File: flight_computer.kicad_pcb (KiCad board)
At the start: 4 copper layers, 95.9 x 90.2 mm, 163 parts, among them J1 436500204, J10 TSW-102-07-F-S, J11 TSW-103-07-F-S, J12 SMA-J-P-H-ST-EM1, J2 0530480210, J3 0530480210, J4 398800302, J5 398800302, J6 398800302, J7 398800302, J8 0530480810, J9 USB4105-GF-A-120, Q6 SI1016CX-T1-GE3, Q7 DMT6007LFGQ-7, U1 STM32F405VGT7, U10 LT6000IDCB#TRMPBF, U11 NC7WZ07P6X, U12 B39162B4300F210, U13 MS561101BA03-50, U14 IAM-20380HT, U15 H3LIS331DLTR, U16 LM74700QDRQ1, U2 INA229AQDGSRQ1, U3 TPS62130AQRGTRQ1, U4 TPS62130AQRGTRQ1, U5 S25FL256LAGNFM010, U6 USBLC6-2P6, U7 MMC5983MA, U8 AIS2IHTR, U9 MAX-M10S-00B, Y1 25MHz

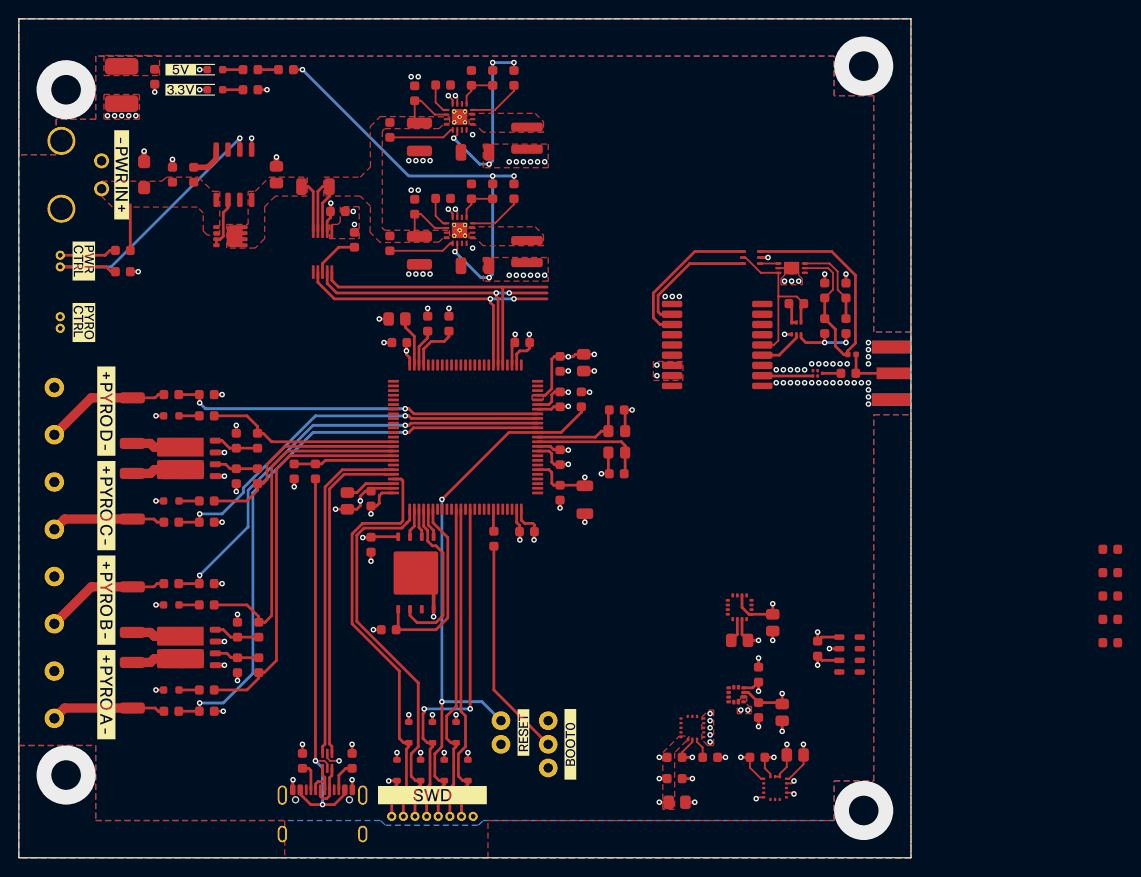
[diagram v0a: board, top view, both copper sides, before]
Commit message: Moved GNSS to bottom right of the board, added sensor ro SPI bus, improved chassis ring to cover more parts of the board
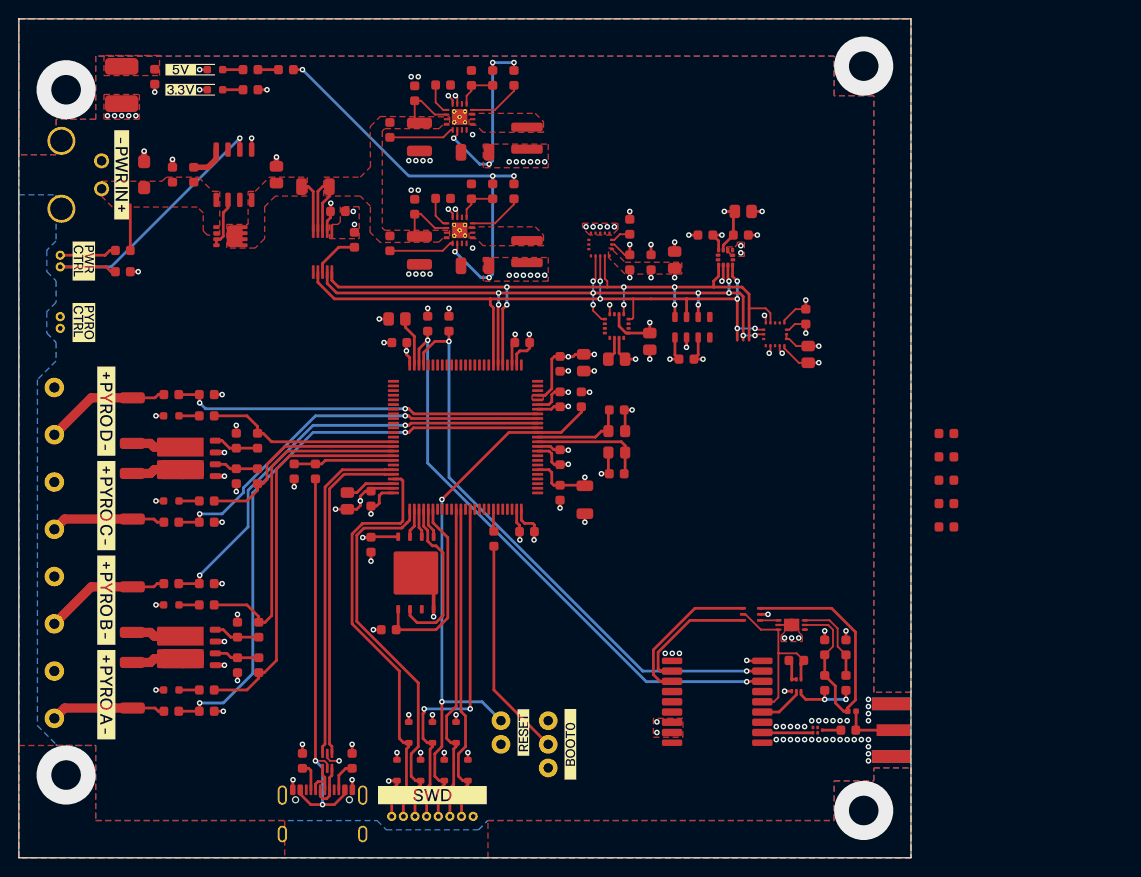
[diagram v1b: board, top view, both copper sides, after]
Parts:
- moved C35 58.3 mm to (175.2, 76.4), turned to 90 degrees
- moved C40 57.7 mm to (170.4, 72.9), turned to 90 degrees
- moved C36 55.6 mm to (172.6, 76.7), turned to 90 degrees
- moved C31 54.0 mm to (182.6, 71.2), turned to 0 degrees
- moved C37 53.4 mm to (170.4, 76.7), turned to 90 degrees
- moved U14 52.9 mm to (167.2, 74.8), turned to 90 degrees
- moved C30 51.1 mm to (182.3, 73.8), turned to 0 degrees
- moved U15 48.8 mm to (186.0, 84.4), turned to -90 degrees
- moved C39 47.7 mm to (189.3, 82.5), turned to -90 degrees
- moved C29 47.6 mm to (178.5, 73.8), turned to 180 degrees
- moved U8 47.0 mm to (180.6, 76.2), turned to 90 degrees
- moved C38 43.1 mm to (189.5, 86.6), turned to -90 degrees
- moved U13 39.0 mm to (177.1, 83.7), turned to 90 degrees
- moved U9 38.4 mm to (179.8, 123.9)
- moved C32 38.4 mm to (191.3, 118.1)
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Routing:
- net I2C2.SDA: track 4.03 -> 63.0 mm, vias 0 -> 2
- net I2C2.SCL: track 5.59 -> 62.6 mm, vias 0 -> 2
- net SPI1.SCLK: track 32.7 -> 75.6 mm, vias 0 -> 6
- net SPI1.MISO: track 33.1 -> 74.5 mm, vias 2 -> 11
- net SPI1.MOSI: track 33.7 -> 74.5 mm, vias 2 -> 6
- net ~{PREC_ACCEL_CS}: track 0.00 -> 1.80 mm, vias 0 -> 1
- net ~{GNSS_SAFEBOOT}: track 0.00 -> 1.69 mm, vias 0 -> 1
- net ~{MAG_CS}: track 0.00 -> 1.02 mm, vias 0 -> 1

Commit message: Added M3 mounting holes to schematic, replaced them in PCB layout so they appear in the output documents
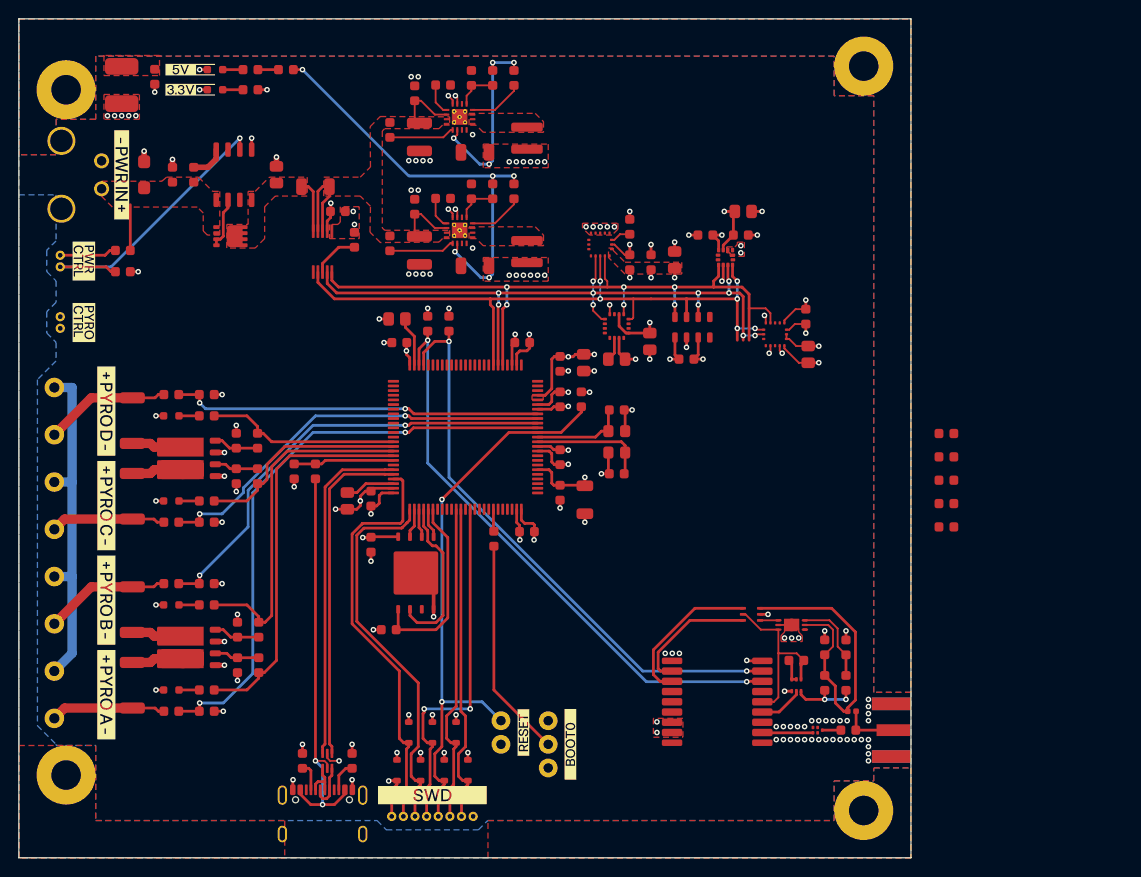
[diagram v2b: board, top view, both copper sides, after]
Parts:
- added MH1: ~, miscellaneous:M3, F.Cu at (195.5, 135.6)
- added MH2: ~, miscellaneous:M3, F.Cu at (109.8, 131.8)
- added MH3: ~, miscellaneous:M3, F.Cu at (109.8, 58.1)
- added MH4: ~, miscellaneous:M3, F.Cu at (195.5, 55.6)
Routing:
- net Net-(J3-Pad2): track 0.00 -> 37.0 mm
- net CHASSIS: vias 4 -> 0
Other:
- board text added: "0,0"
